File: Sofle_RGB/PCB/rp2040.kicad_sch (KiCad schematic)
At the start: 23 parts, among them J100 USB_C_Receptacle_USB2.0

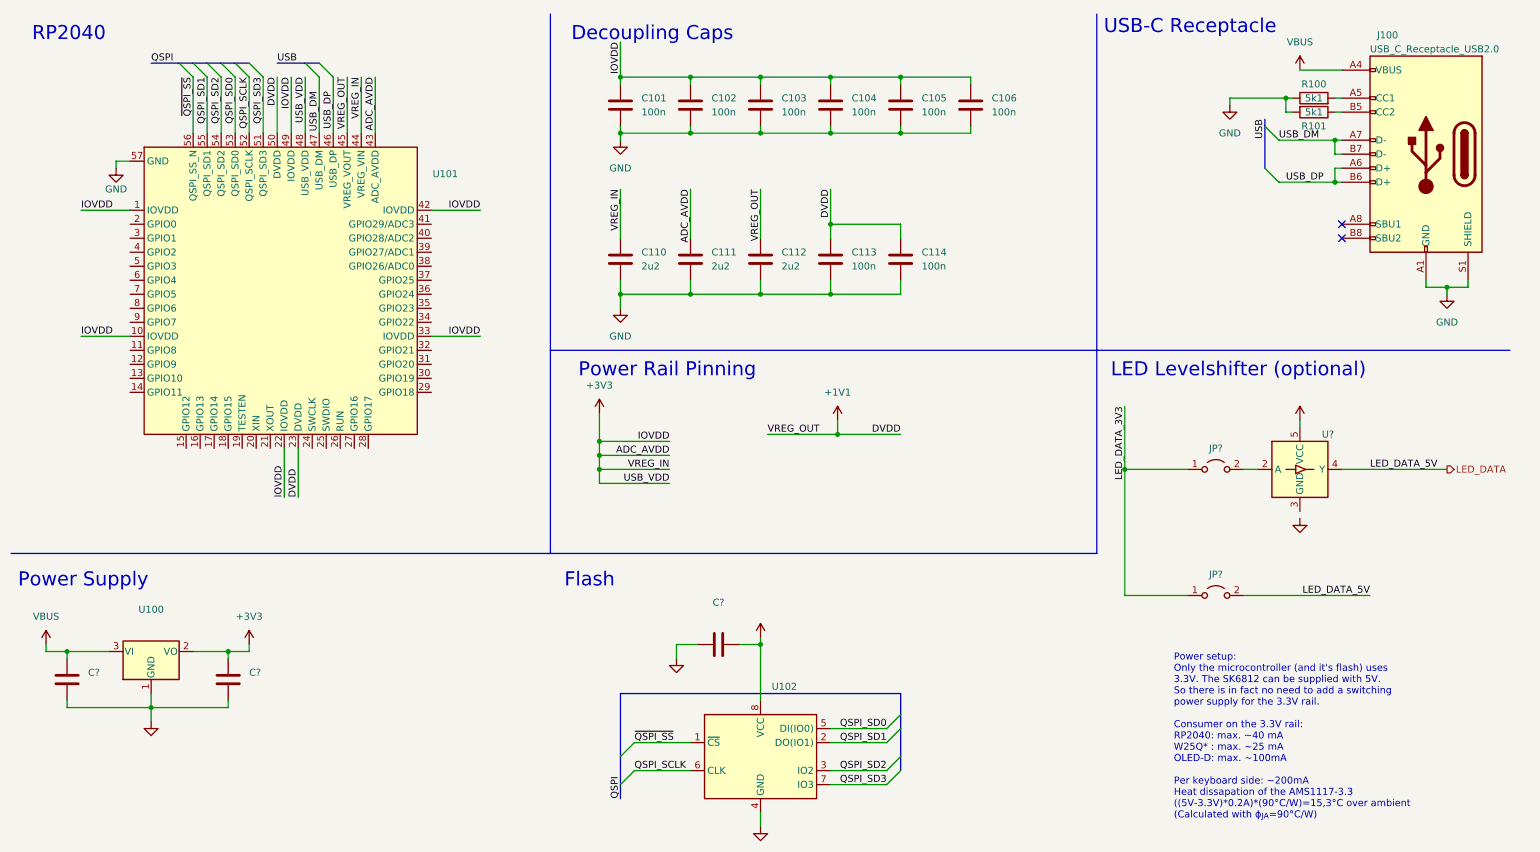
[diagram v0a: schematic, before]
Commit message: RP2040 schematic: - Added Reset and Boot button - Added Crystal - Added Flash - Added (optional) LED level shifter - Rearanged schematic
Main schematic:
- Imported Pins from rp2040 schematic
- Replaced VCC with VBUS representing USB voltage
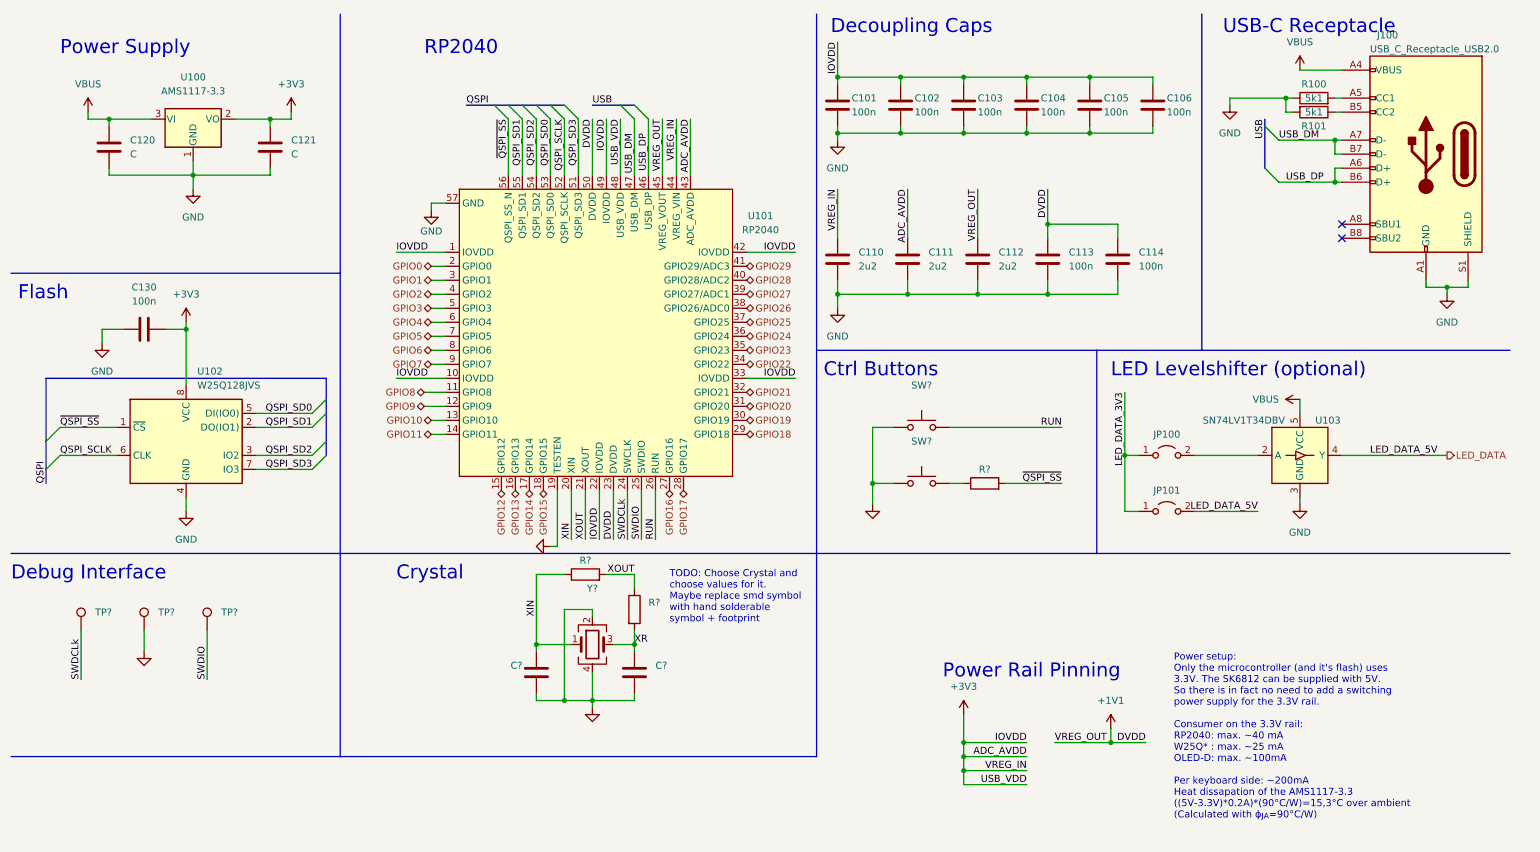
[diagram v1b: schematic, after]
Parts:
- added C? (x2): (no value), symbol Device:C
- added R? (x3): (no value), symbol Device:R
- added SW? (x2): (no value), symbol Switch:SW_Push
- added TP?: (no value), symbol Connector:TestPoint
- added TP? (x2): ~, symbol Connector:TestPoint
- added Y?: (no value), symbol Device:Crystal_GND24
- C120, C121: renamed from C?; value (none) -> C
- C130: renamed from C?; value (none) -> 100n
- JP100: renamed from JP?; value (none) -> Jumper_2_Open; footprint (none) -> Jumper:SolderJumper-2_P1.3mm_Open_RoundedPad1.0x1.5mm
- U100: value (none) -> AMS1117-3.3; footprint (none) -> Package_TO_SOT_SMD:SOT-223-3_TabPin2
- U101: value (none) -> RP2040; footprint (none) -> SofleRGB:QFN-56-1EP_7x7mm_P0.4mm_EP3.2x3.2mm
- U102: value (none) -> W25Q128JVS; footprint (none) -> Package_SO:SOIC-8_5.23x5.23mm_P1.27mm
- U103: renamed from U?; value (none) -> SN74LV1T34DBV; footprint (none) -> Package_TO_SOT_SMD:SOT-23-5
- gave numbers to parts that had none: 1
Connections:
- net GND: now also U101.19 (TESTEN), U103.3 (GND), C?.1, C?.2, SW?.1, SW?.1, TP?.1, Y?.2, Y?.4
- net ~{QSPI_SS}: now also R?.2
- net GPIO8: now reaches U101.11 (GPIO8)
- net GPIO9: now reaches U101.12 (GPIO9)
- net GPIO10: now reaches U101.13 (GPIO10)
- net GPIO11: now reaches U101.14 (GPIO11)
- net GPIO12: now reaches U101.15 (GPIO12)
- net GPIO13: now reaches U101.16 (GPIO13)
- net GPIO14: now reaches U101.17 (GPIO14)
- net GPIO15: now reaches U101.18 (GPIO15)
- net GPIO0: now reaches U101.2 (GPIO0)
- net XIN: now reaches U101.20 (XIN)
- net XIN: now also C?.2, R?.1, Y?.1
- net XOUT: now reaches U101.21 (XOUT)
- net XOUT: now also R?.1, R?.2
- net SWDCLk: now reaches U101.24 (SWCLK)
- net SWDCLk: now also TP?.1
- net SWDIO: now reaches U101.25 (SWDIO)
- net SWDIO: now also TP?.1
- net RUN: now reaches U101.26 (RUN)
- net RUN: now also SW?.2
- net GPIO16: now reaches U101.27 (GPIO16)
- net GPIO17: now reaches U101.28 (GPIO17)
- net GPIO18: now reaches U101.29 (GPIO18)
- net GPIO1: now reaches U101.3 (GPIO1)
- net GPIO19: now reaches U101.30 (GPIO19)
- net GPIO20: now reaches U101.31 (GPIO20)
- net GPIO21: now reaches U101.32 (GPIO21)
- net GPIO22: now reaches U101.34 (GPIO22)
- net GPIO23: now reaches U101.35 (GPIO23)
- net GPIO24: now reaches U101.36 (GPIO24)
- net GPIO25: now reaches U101.37 (GPIO25)
- net GPIO26: now reaches U101.38 (GPIO26/ADC0)
- net GPIO27: now reaches U101.39 (GPIO27/ADC1)
- net GPIO2: now reaches U101.4 (GPIO2)
- net GPIO28: now reaches U101.40 (GPIO28/ADC2)
- net GPIO29: now reaches U101.41 (GPIO29/ADC3)
- net GPIO3: now reaches U101.5 (GPIO3)
- net GPIO4: now reaches U101.6 (GPIO4)
- net GPIO5: now reaches U101.7 (GPIO5)
- net GPIO6: now reaches U101.8 (GPIO6)
- net GPIO7: now reaches U101.9 (GPIO7)
- new net: R?.1, SW?.2
- new net XR: C?.1, R?.2, Y?.3
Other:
- note added: "Crystal"
- note added: "Ctrl Buttons"
- note added: "Debug Interface"
- note added: "TODO: Choose Crystal and choose values for it. Maybe replace smd symbol with hand solderable symbol + footprint"
- moved on the sheet: C101, C102, C103, C104, C105, C106, C110, C111, C112, C113, C114, C120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
